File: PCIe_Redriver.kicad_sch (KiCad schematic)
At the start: 51 parts, among them U10 SN75LVPE4410RNQR, U9 SN75LVPE4410RNQR

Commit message: Updated schematics
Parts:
- removed C50: 10μF, symbol Device:C
- added R65, R66, R67, R68, R69, R70, R71, R72, R73, R74: 3k, Resistor_SMD:R_0603_1608Metric, symbol Device:R_Small
- C51, C52: value 1.0μF -> 1µF; footprint (none) -> Capacitor_SMD:C_0603_1608Metric; LCSC (none) -> C15849; Part_Number (none) -> CL10A105KB8NNNC
- C53, C54, C59, C60: footprint (none) -> Capacitor_SMD:C_0402_1005Metric; LCSC (none) -> C1525; Part_Number (none) -> CL05B104KO5NNNC
- C55, C56, C57, C58, C61, C62, C63, C64: footprint (none) -> Capacitor_SMD:C_0603_1608Metric_Pad1.08x0.95mm_HandSolder; LCSC (none) -> C14663; Part_Number (none) -> CC0603KRX7R9BB104
- C75, C76, C77, C78, C79, C80, C81, C82, C83, C84, C85, C86, C87, C88, C89, C90: value 0.1µF -> 220nF; footprint Capacitor_SMD:C_0201_0603Metric -> Capacitor_SMD:C_0402_1005Metric; LCSC C160831 -> C16772; Part_Number CL03A104KQ3NNNC -> CL05B224KO5NNNC
- R32, R33, R34, R50, R58, R59: LCSC C105870 -> C25900; Part_Number RC0402JR-074K7L -> 0402WGF4701TCE
- R35, R51: footprint (none) -> Resistor_SMD:R_0402_1005Metric; LCSC (none) -> C11702; Part_Number (none) -> 0402WGF1001TCE
- R38, R43, R44, R48, R49, R53, R54, R55, R56, R57: value 59k -> 56k; footprint (none) -> Resistor_SMD:R_0402_1005Metric; symbol Device:R -> Device:R_Small; LCSC (none) -> C25796; Part_Number (none) -> 0402WGF5602TCE
- U10, U9: LCSC (none) -> C2876351; Part_Number (none) -> SN75LVPE4410RNQR
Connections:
- net GND: now also R65.2, R66.2, R67.2, R68.2, R69.2, R70.2, R71.2, R72.2, R73.2, R74.2; no longer R38.2, R43.2, R44.2, R48.2, R49.2, R53.2, R54.2, R55.2, R56.2, R57.2
- net TX3CP: now reaches C84.2, U10.10 (TX3P)
- net TX1CP: now reaches C86.2, U10.17 (TX1P)
- net TX4CN: now reaches C75.2, U9.19 (TX0N)
- net TX7CP: now reaches C82.2, U9.10 (TX3P)
- net TX6CN: now reaches C79.2, U9.12 (TX2N)
- net TX6CP: now reaches C80.2, U9.13 (TX2P)
- net TX5CN: now reaches C77.2, U9.16 (TX1N)
- net TX5CP: now reaches C78.2, U9.17 (TX1P)
- net TX4CP: now reaches C76.2, U9.20 (TX0P)
- net TX7CN: now reaches C81.2, U9.9 (TX3N)
- net TX2CN: now reaches C87.2, U10.12 (TX2N)
- net TX2CP: now reaches C88.2, U10.13 (TX2P)
- net TX3CN: now reaches C83.2, U10.9 (TX3N)
- net TX1CN: now reaches C85.2, U10.16 (TX1N)
- net TX0CN: now reaches C89.2, U10.19 (TX0N)
- net TX0CP: now reaches C90.2, U10.20 (TX0P)
- new net: R56.2, R72.1
- new net: R43.2, R68.1
- new net: R53.2, R71.1
- new net: R38.2, R66.1
- new net: R48.2, R67.1
- new net: R54.2, R73.1
- new net: R57.2, R74.1
- new net: R44.2, R65.1
- new net: R55.2, R70.1
- new net: R49.2, R69.1
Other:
- moved on the sheet: R43, R44, R49, R54, R55, R57

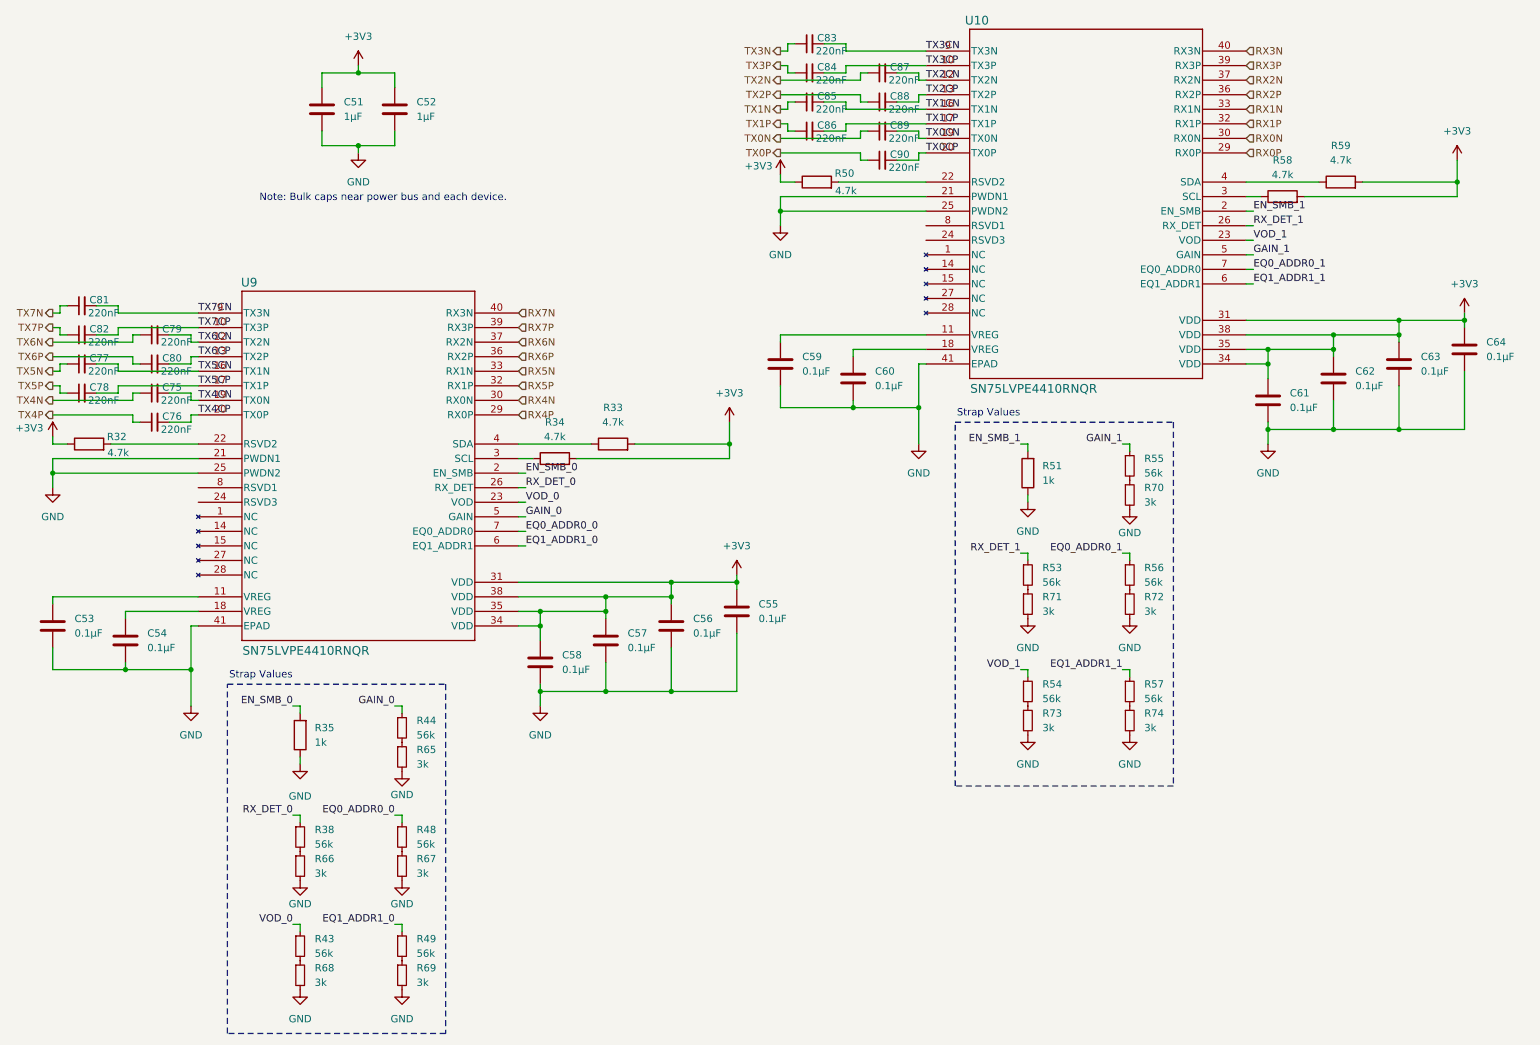
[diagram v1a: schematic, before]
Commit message: Lay out more components
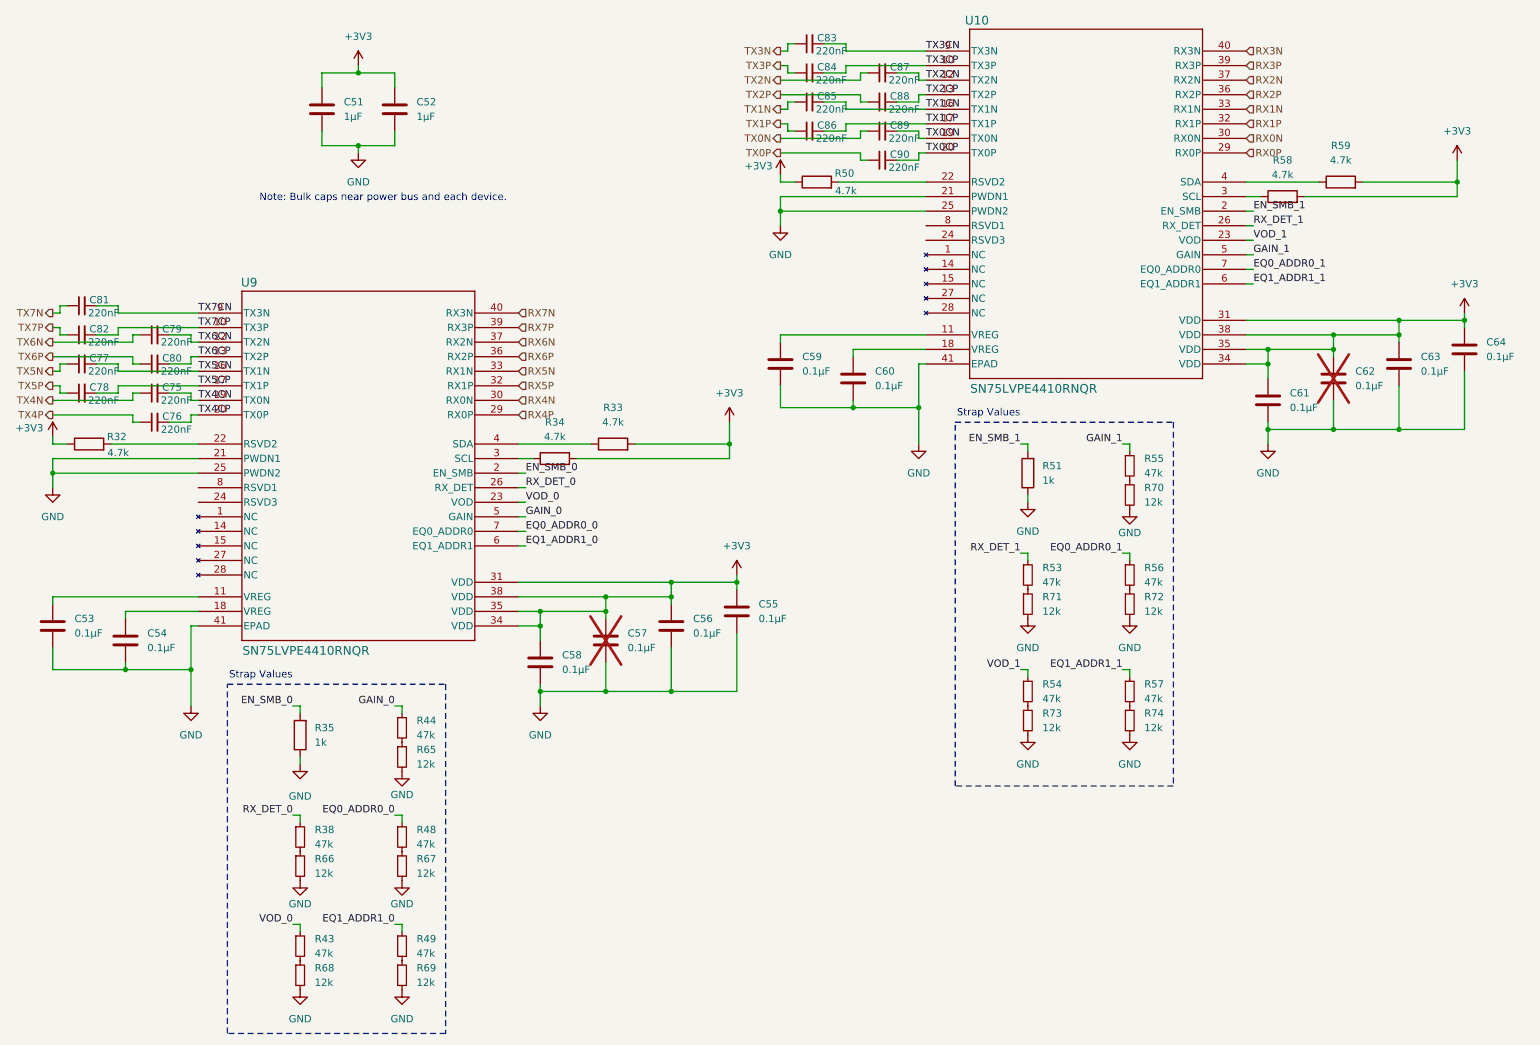
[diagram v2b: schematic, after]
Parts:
- C55, C56, C58, C61, C63, C64: footprint Capacitor_SMD:C_0603_1608Metric_Pad1.08x0.95mm_HandSolder -> Capacitor_SMD:C_0402_1005Metric; LCSC C14663 -> C1525; Part_Number CC0603KRX7R9BB104 -> CL05B104KO5NNNC
- C57, C62: footprint Capacitor_SMD:C_0603_1608Metric_Pad1.08x0.95mm_HandSolder -> Capacitor_SMD:C_0402_1005Metric; LCSC C14663 -> C1525; Part_Number CC0603KRX7R9BB104 -> CL05B104KO5NNNC; now not fitted; now left out of the parts list
- R38, R43, R44, R48, R49, R53, R54, R55, R56, R57: value 56k -> 47k; LCSC C25796 -> C25792; Part_Number 0402WGF5602TCE -> 0402WGF4702TCE
- R65, R66, R67, R68, R69, R70, R71, R72, R73, R74: value 3k -> 12k; footprint Resistor_SMD:R_0603_1608Metric -> Resistor_SMD:R_0402_1005Metric; LCSC C4211 -> C25752; Part_Number 0603WAF3001T5E -> 0402WGF1202TCE

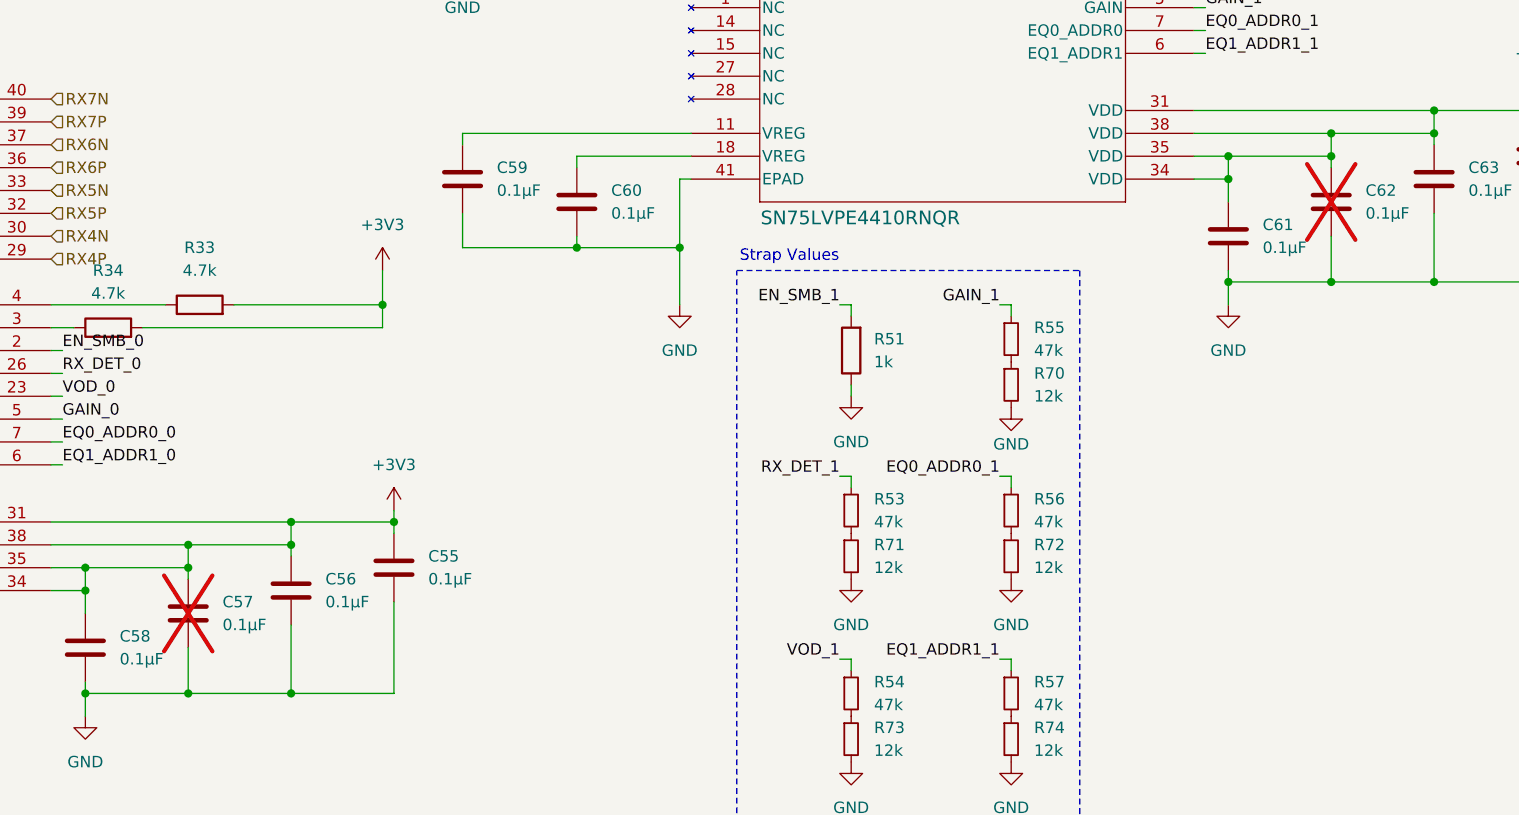
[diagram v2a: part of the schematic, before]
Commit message: Rewired PCIe without redriver
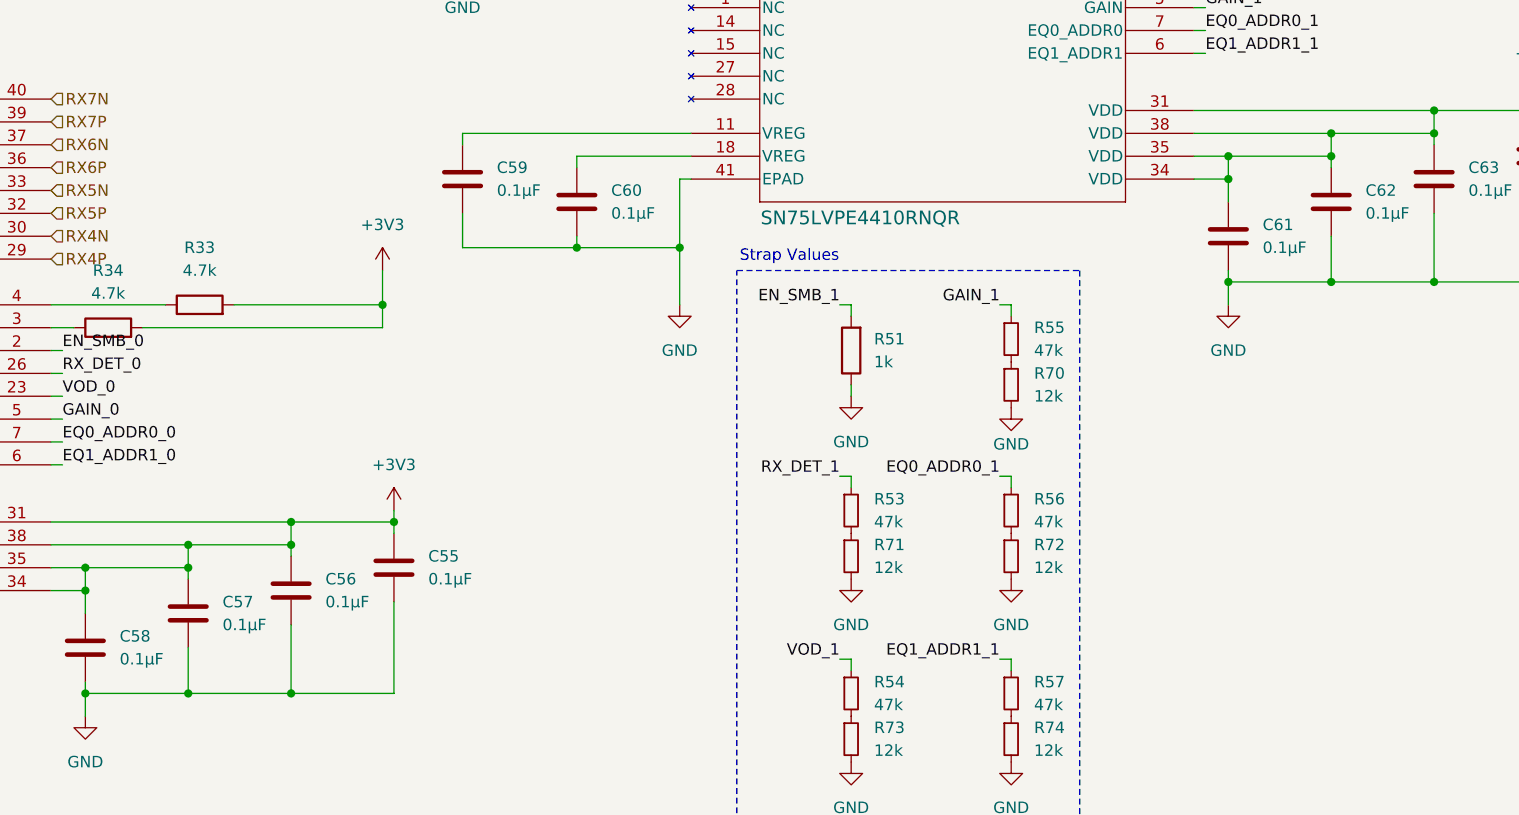
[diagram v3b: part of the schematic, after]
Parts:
- C57, C62: now fitted; now in the parts list
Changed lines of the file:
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@@
 		(unit 1)
 		(exclude_from_sim no)
-		(in_bom no)
-		(on_board no)
-		(dnp yes)
+		(in_bom yes)
+		(on_board yes)
+		(dnp no)
 		(fields_autoplaced yes)
 		(property "Reference" "C57"
@@
 		(unit 1)
 		(exclude_from_sim no)
-		(in_bom no)
-		(on_board no)
-		(dnp yes)
+		(in_bom yes)
+		(on_board yes)
+		(dnp no)
 		(fields_autoplaced yes)
 		(property "Reference" "C62"

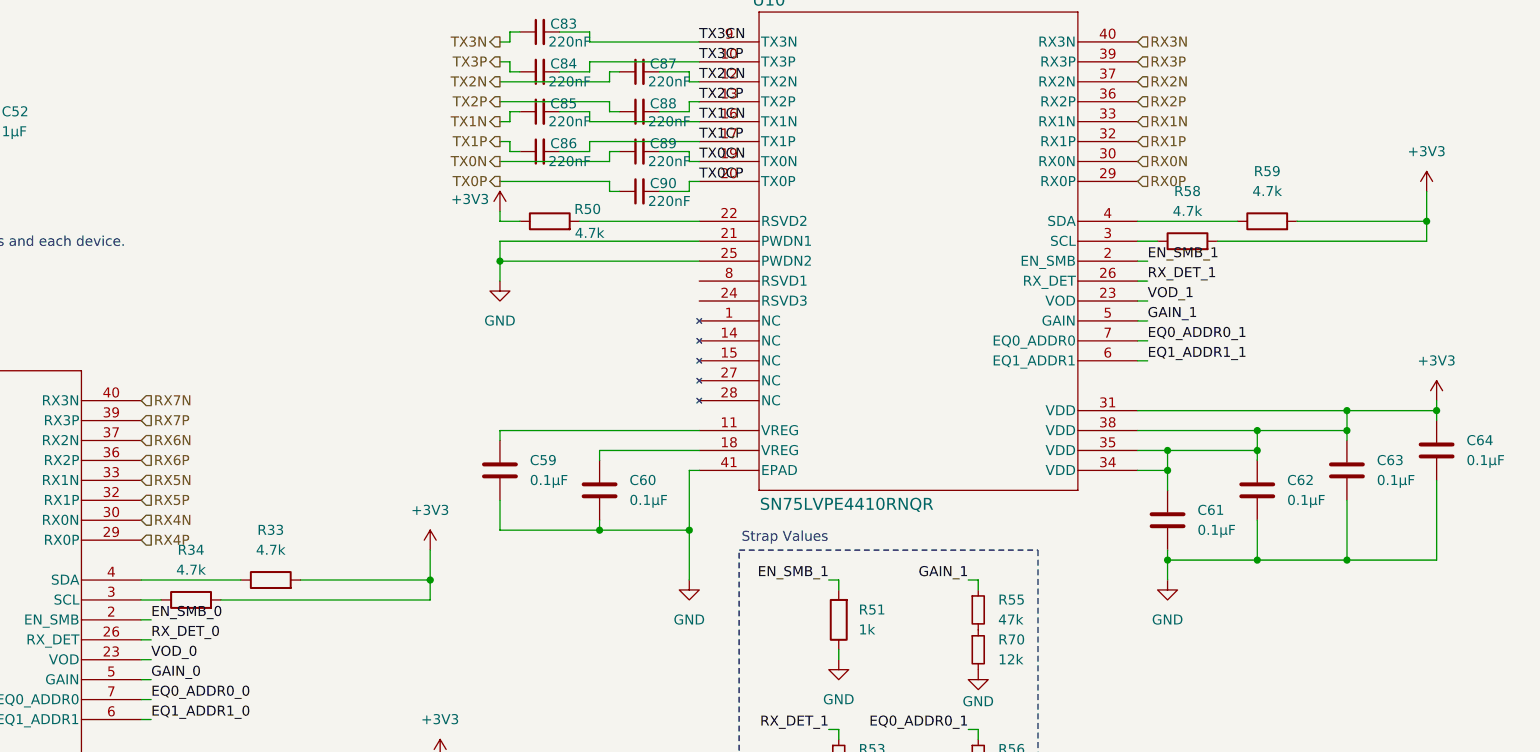
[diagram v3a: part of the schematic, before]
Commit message: Added MCU
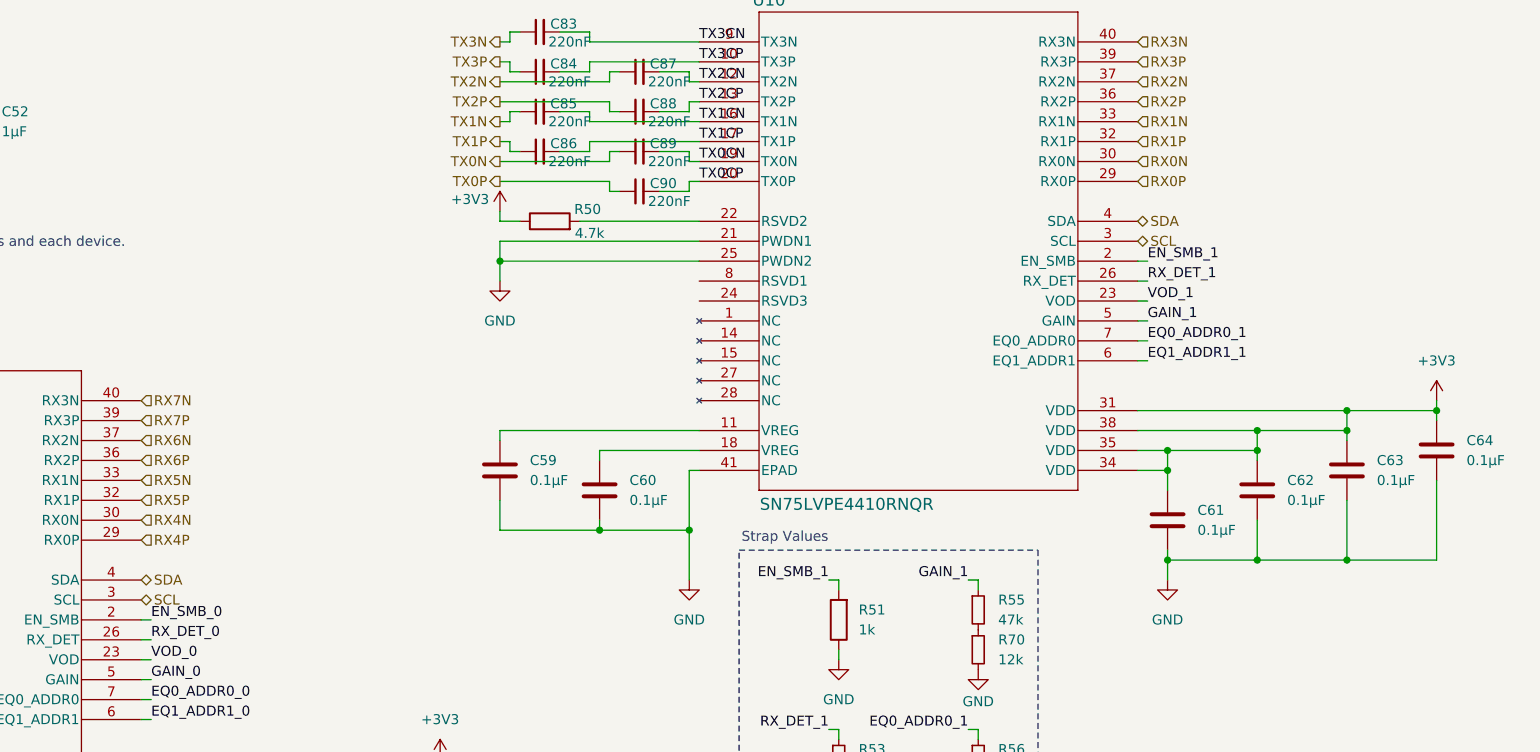
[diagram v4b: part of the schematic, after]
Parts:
- removed R33, R34, R58, R59: 4.7k, Resistor_SMD:R_0402_1005Metric, symbol Device:R
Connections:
- net SCL: now reaches U9.3 (SCL)
- net SCL: now also U10.3 (SCL)
- net SDA: now reaches U9.4 (SDA)
- net SDA: now also U10.4 (SDA)
